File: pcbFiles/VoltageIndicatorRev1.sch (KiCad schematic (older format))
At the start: 6 parts

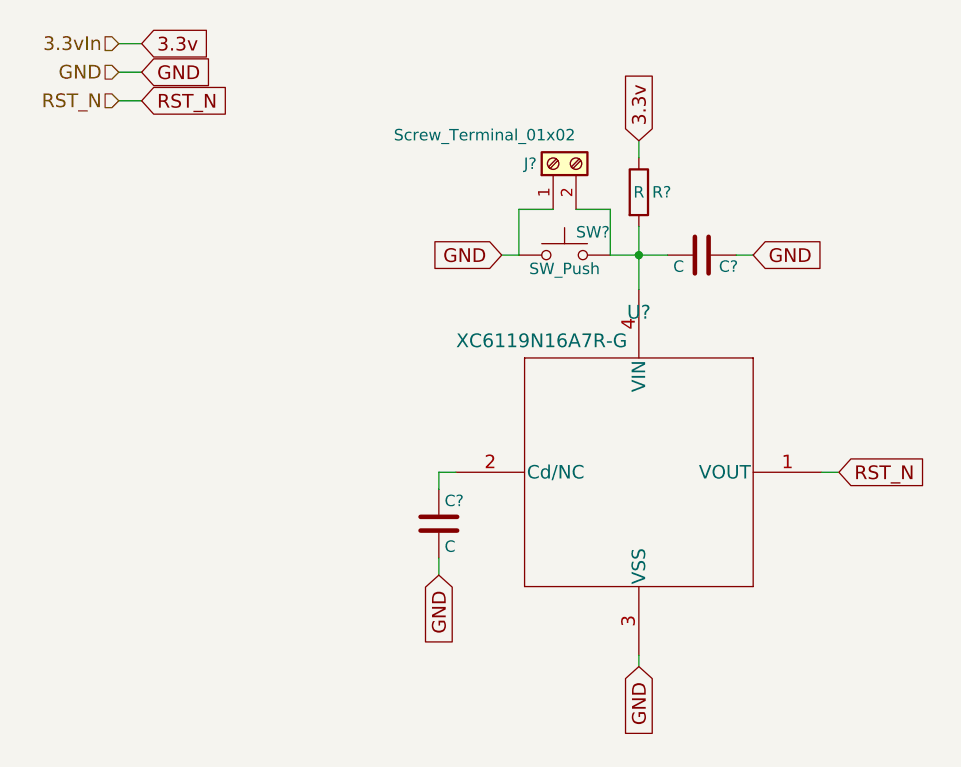
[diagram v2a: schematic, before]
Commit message: Update Footprints and Board Layers
Still need to get foorprint for x... device and the lpf may need to make them if I cannot find them @willcarroll7
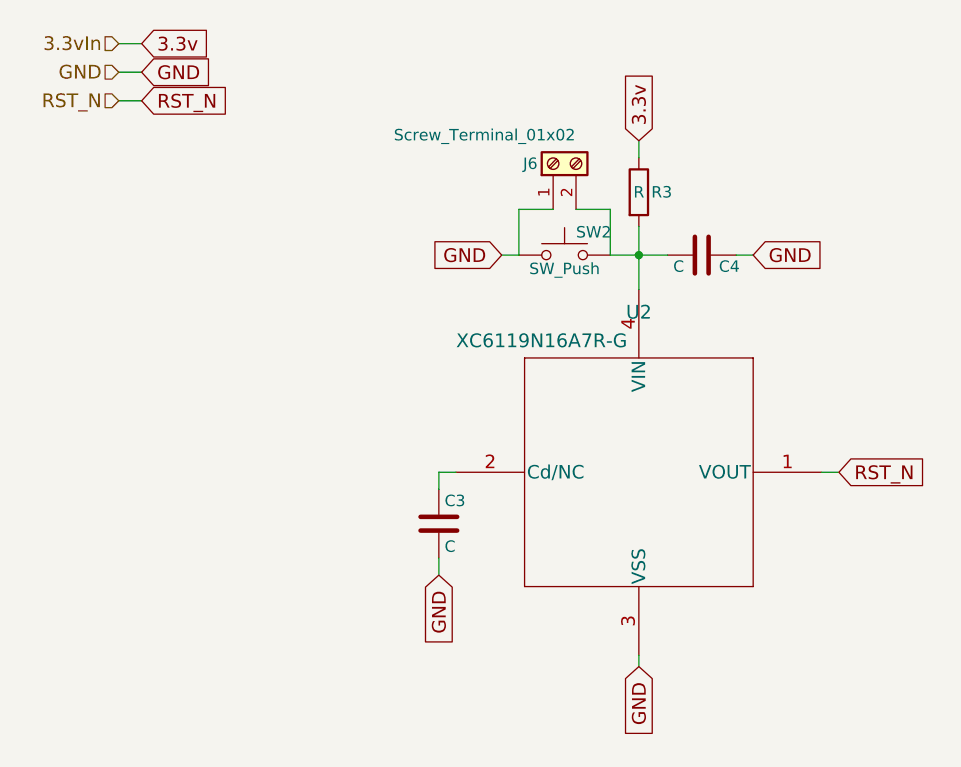
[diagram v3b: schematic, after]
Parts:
- C3, C4: renamed from C?; footprint (none) -> Capacitors_SMD:C_0402
- J6: renamed from J?; footprint (none) -> Pin_Headers:Pin_Header_Straight_1x02_Pitch2.54mm
- R3: renamed from R?; footprint (none) -> Resistors_SMD:R_0402
- SW2: renamed from SW?; footprint (none) -> Buttons_Switches_SMD:SW_DIP_x1_W8.61mm_Slide_LowProfile
- gave numbers to parts that had none: 1
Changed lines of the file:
@@
-EESchema Schematic File Version 4
+EESchema Schematic File Version 2
 LIBS:power
+LIBS:device
+LIBS:switches
+LIBS:relays
+LIBS:motors
+LIBS:transistors
+LIBS:conn
+LIBS:linear
+LIBS:regul
 LIBS:74xx
+LIBS:cmos4000
+LIBS:adc-dac
+LIBS:memory
+LIBS:xilinx
+LIBS:microcontrollers
+LIBS:dsp
+LIBS:microchip
+LIBS:analog_switches
+LIBS:motorola
+LIBS:texas
+LIBS:intel
+LIBS:audio
+LIBS:interface
+LIBS:digital-audio
+LIBS:philips
+LIBS:display
+LIBS:cypress
+LIBS:siliconi
+LIBS:opto
+LIBS:atmel
+LIBS:contrib
+LIBS:valves
+LIBS:ADS1115IDGST
+LIBS:CYW20719B1KUMLG
+LIBS:LSM9DS1TR
+LIBS:TPS63001DRCT
+LIBS:MCP73831T-2ACI_OT
+LIBS:A-1JB
+LIBS:XC6119N16A7R-G
 LIBS:GolfGloveMainBoardV1.0.0-cache
-EELAYER 26 0
+EELAYER 25 0
 EELAYER END
 $Descr A4 11693 8268
@@
 $EndDescr
 $Comp
-L XC6119N16A7R-G U?
+L XC6119N16A7R-G U2
 U 1 1 5C49E973
 P 4700 3500
-F 0 "U?" H 5500 4200 60  0000 C CNN
+F 0 "U2" H 5500 4200 60  0000 C CNN
 F 1 "XC6119N16A7R-G" H 5075 4075 60  0000 C CNN
 F 2 "XC6119_USPN-4" H 5500 4040 60  0001 C CNN
@@
 $EndComp
 $Comp
-L SW_Push SW?
+L SW_Push SW2
 U 1 1 5C49E9D3
 P 5175 2550
-F 0 "SW?" H 5225 2650 50  0000 L CNN
+F 0 "SW2" H 5225 2650 50  0000 L CNN
 F 1 "SW_Push" H 5175 2490 50  0000 C CNN
-F 2 "" H 5175 2750 50  0001 C CNN
+F 2 "Buttons_Switches_SMD:SW_DIP_x1_W8.61mm_Slide_LowProfile" H 5175 2750 50  0001 C CNN
 F 3 "" H 5175 2750 50  0001 C CNN
 	1    5175 2550
@@
 $EndComp
 $Comp
-L R R?
+L R R3
 U 1 1 5C49EA34
 P 5500 2275
-F 0 "R?" H 5600 2275 50  0000 C CNN
+F 0 "R3" H 5600 2275 50  0000 C CNN
 F 1 "R" H 5500 2275 50  0000 C CNN
-F 2 "" V 5430 2275 50  0001 C CNN
+F 2 "Resistors_SMD:R_0402" V 5430 2275 50  0001 C CNN
 F 3 "" H 5500 2275 50  0001 C CNN
 	1    5500 2275
@@
 $EndComp
 $Comp
-L C C?
+L C C4
 U 1 1 5C49EB39
 P 5775 2550
-F 0 "C?" V 5825 2625 50  0000 L CNN
+F 0 "C4" V 5825 2625 50  0000 L CNN
 F 1 "C" V 5825 2425 50  0000 L CNN
-F 2 "" H 5813 2400 50  0001 C CNN
+F 2 "Capacitors_SMD:C_0402" H 5813 2400 50  0001 C CNN
 F 3 "" H 5775 2550 50  0001 C CNN
 	1    5775 2550
@@
 $EndComp
 $Comp
-L C C?
+L C C3
 U 1 1 5C49EC00
 P 4625 3725
-F 0 "C?" H 4650 3825 50  0000 L CNN
+F 0 "C3" H 4650 3825 50  0000 L CNN
 F 1 "C" H 4650 3625 50  0000 L CNN
-F 2 "" H 4663 3575 50  0001 C CNN
+F 2 "Capacitors_SMD:C_0402" H 4663 3575 50  0001 C CNN
 F 3 "" H 4625 3725 50  0001 C CNN
 	1    4625 3725
@@
 	5925 2550 6000 2550
 $Comp
-L Screw_Terminal_01x02 J?
+L Screw_Terminal_01x02 J6
 U 1 1 5C49F0AE
 P 5125 2150
-F 0 "J?" V 5125 2250 50  0000 C CNN
+F 0 "J6" V 5125 2250 50  0000 C CNN
 F 1 "Screw_Terminal_01x02" V 5250 2450 50  0000 C CNN
-F 2 "" H 5125 2150 50  0001 C CNN
+F 2 "Pin_Headers:Pin_Header_Straight_1x02_Pitch2.54mm" H 5125 2150 50  0001 C CNN
 F 3 "" H 5125 2150 50  0001 C CNN
 	1    5125 2150

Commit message: Update the Voltage Detector Footprint
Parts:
- SW2: footprint Buttons_Switches_SMD:SW_DIP_x1_W8.61mm_Slide_LowProfile -> Buttons_Switches_SMD:Panasonic_EVQPUL_EVQPUC
- U2: footprint XC6119_USPN-4 -> DFN-4-------------------------:DFN-4
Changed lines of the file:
@@
 F 0 "U2" H 5500 4200 60  0000 C CNN
 F 1 "XC6119N16A7R-G" H 5075 4075 60  0000 C CNN
-F 2 "XC6119_USPN-4" H 5500 4040 60  0001 C CNN
+F 2 "DFN-4-------------------------:DFN-4" H 5500 4040 60  0001 C CNN
 F 3 "" H 4700 3500 60  0000 C CNN
 	1    4700 3500
@@
 F 0 "SW2" H 5225 2650 50  0000 L CNN
 F 1 "SW_Push" H 5175 2490 50  0000 C CNN
-F 2 "Buttons_Switches_SMD:SW_DIP_x1_W8.61mm_Slide_LowProfile" H 5175 2750 50  0001 C CNN
+F 2 "Buttons_Switches_SMD:Panasonic_EVQPUL_EVQPUC" H 5175 2750 50  0001 C CNN
 F 3 "" H 5175 2750 50  0001 C CNN
 	1    5175 2550

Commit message: Update Circuit With Antenna
This commit will update the pcb with a mock up of the antenna design without the vias, this commit will also update the pressure sensors to be attached to the top of hand unit to allow for USB-C Connection. @willcarroll7
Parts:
- SW2: footprint Buttons_Switches_SMD:Panasonic_EVQPUL_EVQPUC -> Buttons_Switches_SMD:SW_DIP_x1_W8.61mm_Slide_LowProfile
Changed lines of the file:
@@
 LIBS:valves
 LIBS:2450AT42B100E
+LIBS:A-1JB
+LIBS:ADS1115IDGST
+LIBS:CD4011BM96
+LIBS:CYW20719B1KUMLG
+LIBS:LSM9DS1TR
+LIBS:MCP73831T-2ACI_OT
+LIBS:MMDT3904V-7
+LIBS:MMPQ3904
+LIBS:S2B-PH-K-S_LF__SN_
+LIBS:TPS63001DRCT
+LIBS:XC6119N16A7R-G
 LIBS:GolfGloveMainBoardV1.0.0-cache
 EELAYER 25 0
@@
 F 0 "SW2" H 5225 2650 50  0000 L CNN
 F 1 "SW_Push" H 5175 2490 50  0000 C CNN
-F 2 "Buttons_Switches_SMD:Panasonic_EVQPUL_EVQPUC" H 5175 2750 50  0001 C CNN
+F 2 "Buttons_Switches_SMD:SW_DIP_x1_W8.61mm_Slide_LowProfile" H 5175 2750 50  0001 C CNN
 F 3 "" H 5175 2750 50  0001 C CNN
 	1    5175 2550

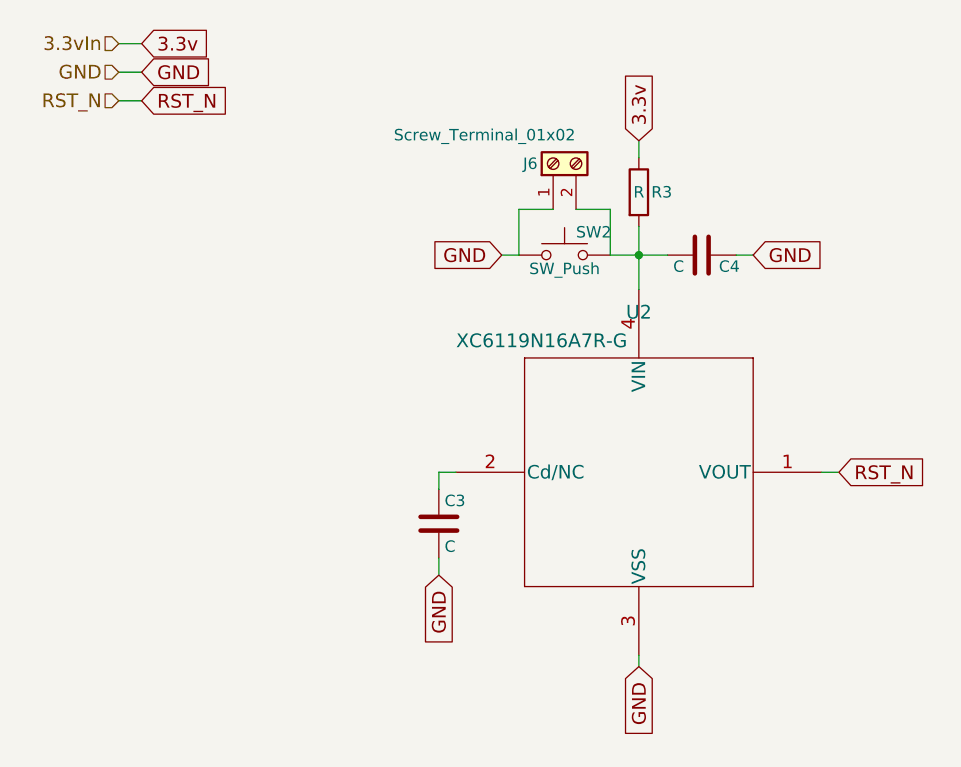
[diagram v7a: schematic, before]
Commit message: Update Board Files
Updated schematic files, completed REV1.0 of the board design, waiting for review by @willcarroll7
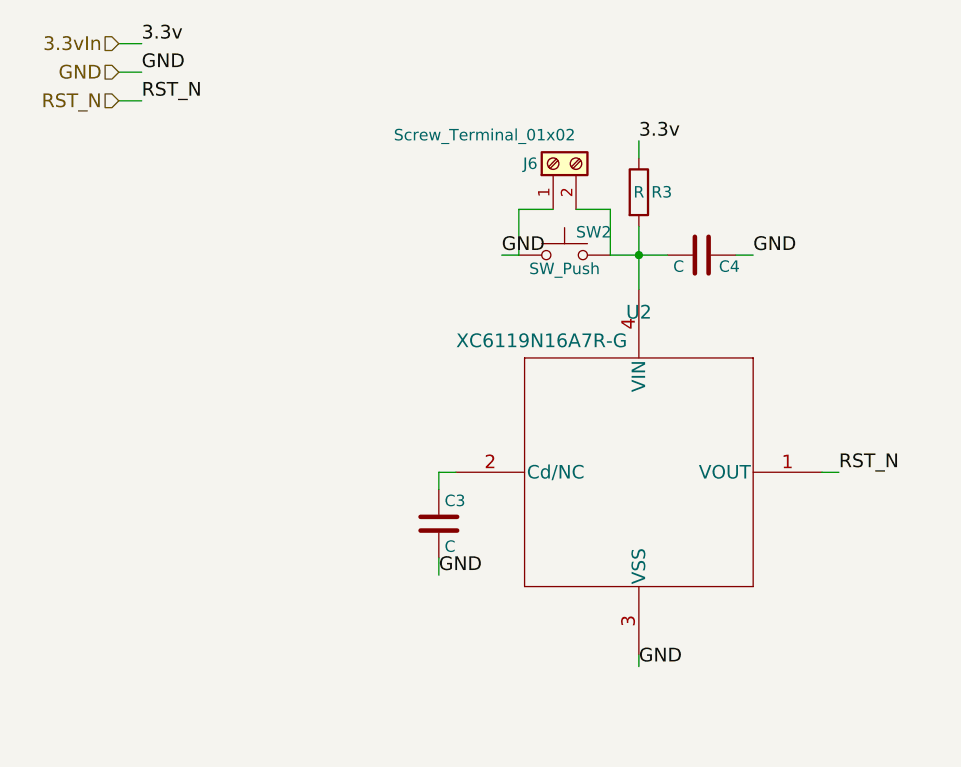
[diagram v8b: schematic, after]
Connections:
- net 3.3v renamed 3.3vIn
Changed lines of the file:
@@
 LIBS:contrib
 LIBS:valves
-LIBS:2450AT42B100E
-LIBS:A-1JB
 LIBS:ADS1115IDGST
-LIBS:CD4011BM96
 LIBS:CYW20719B1KUMLG
 LIBS:LSM9DS1TR
+LIBS:TPS63001DRCT
 LIBS:MCP73831T-2ACI_OT
+LIBS:A-1JB
+LIBS:XC6119N16A7R-G
+LIBS:2450AT42B100E
+LIBS:CD4011BM96
 LIBS:MMDT3904V-7
 LIBS:MMPQ3904
 LIBS:S2B-PH-K-S_LF__SN_
-LIBS:TPS63001DRCT
-LIBS:XC6119N16A7R-G
 LIBS:GolfGloveMainBoardV1.0.0-cache
 EELAYER 25 0
@@
 Text HLabel 3225 1875 0    60   Input ~ 0
 RST_N
-Text GLabel 3325 1875 2    60   Input ~ 0
-RST_N
-Text GLabel 3325 1750 2    60   Input ~ 0
-GND
-Text GLabel 3325 1625 2    60   Input ~ 0
-3.3v
 Wire Wire Line
 	3225 1625 3325 1625
@@
 Wire Wire Line
 	3225 1875 3325 1875
-Text GLabel 5500 2050 1    60   Input ~ 0
-3.3v
-Text GLabel 4625 3950 3    60   Input ~ 0
-GND
-Text GLabel 4900 2550 0    60   Input ~ 0
-GND
-Text GLabel 6375 3500 2    60   Input ~ 0
-RST_N
 Wire Wire Line
 	6375 3500 6300 3500
-Text GLabel 5500 4350 3    60   Input ~ 0
-GND
 Wire Wire Line
 	5500 4300 5500 4350
@@
 Wire Wire Line
 	4625 3500 4625 3575
-Text GLabel 6000 2550 2    60   Input ~ 0
-GND
 Wire Wire Line
 	4900 2550 4975 2550
@@
 Wire Wire Line
 	5375 2350 5375 2550
+Text Label 3325 1625 0    60   ~ 0
+3.3v
+Text Label 3325 1750 0    60   ~ 0
+GND
+Text Label 3325 1875 0    60   ~ 0
+RST_N
+Text Label 4625 3950 0    60   ~ 0
+GND
+Text Label 5500 4350 0    60   ~ 0
+GND
+Text Label 6375 3500 0    60   ~ 0
+RST_N
+Text Label 6000 2550 0    60   ~ 0
+GND
+Text Label 5500 2050 0    60   ~ 0
+3.3v
+Text Label 4900 2550 0    60   ~ 0
+GND
 $EndSCHEMATC
